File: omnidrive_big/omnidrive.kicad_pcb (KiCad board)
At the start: 2 copper layers, 165 x 87.9 mm, 73 parts, among them U1 TL072, U2 TL072

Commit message: Latest updates
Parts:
- moved R15 2.90 mm to (84.1, 49.1)
- moved R22 2.90 mm to (66.3, 48.8)
- moved R8 2.90 mm to (53.7, 57.3)
- moved C13 2.90 mm to (59.2, 55.0)
- moved R2 2.90 mm to (23.6, 56.6)
- moved R3 2.90 mm to (28.4, 49.0)
- moved R4 2.90 mm to (32.5, 49.0)
- moved R5 2.90 mm to (36.6, 56.6)
- moved U1 2.90 mm to (42.0, 49.3)
- moved U2 2.90 mm to (72.1, 49.1)
- moved J_OUT_SLV1 1.48 mm to (123.8, 56.1)
- moved J_IN_SLV1 1.45 mm to (24.0, 23.6)
- moved C7 1.30 mm to (117.5, 52.3)
- moved R16 1.30 mm to (105.5, 56.4)
- moved R19 1.30 mm to (110.4, 48.8)
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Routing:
- net Net-(J_GAIN_1-Pin_1): track 0.00 -> 90.8 mm
- net Net-(J_BLEND_2-Pin_1): track 0.00 -> 89.4 mm
- net +9V: track 0.00 -> 86.8 mm, vias 0 -> 1
- net GND: track 0.00 -> 73.6 mm, vias 0 -> 7
- net Net-(J_BLEND_3-Pin_1): track 0.00 -> 71.9 mm
- net /Vb: track 0.00 -> 57.5 mm
- net Net-(J_GAIN_2-Pin_1): track 0.00 -> 50.2 mm, vias 0 -> 1
- net Net-(J_BOOST_3-Pin_1): track 0.00 -> 43.8 mm
- net Net-(U1B-+): track 0.00 -> 39.7 mm
- net Net-(J_MODE_2-Pin_1): track 0.00 -> 38.8 mm, vias 0 -> 1
- net Net-(J_FILT_1-Pin_1): track 0.00 -> 37.3 mm
- net Net-(J_TONE_1-Pin_1): track 0.00 -> 36.4 mm
- net Net-(J_FILT_2-Pin_1): track 0.00 -> 36.3 mm
- net Net-(D1-A): track 0.00 -> 35.7 mm
- net Net-(U1B--): track 0.00 -> 34.6 mm
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- added copper zone on F.Cu, net GND

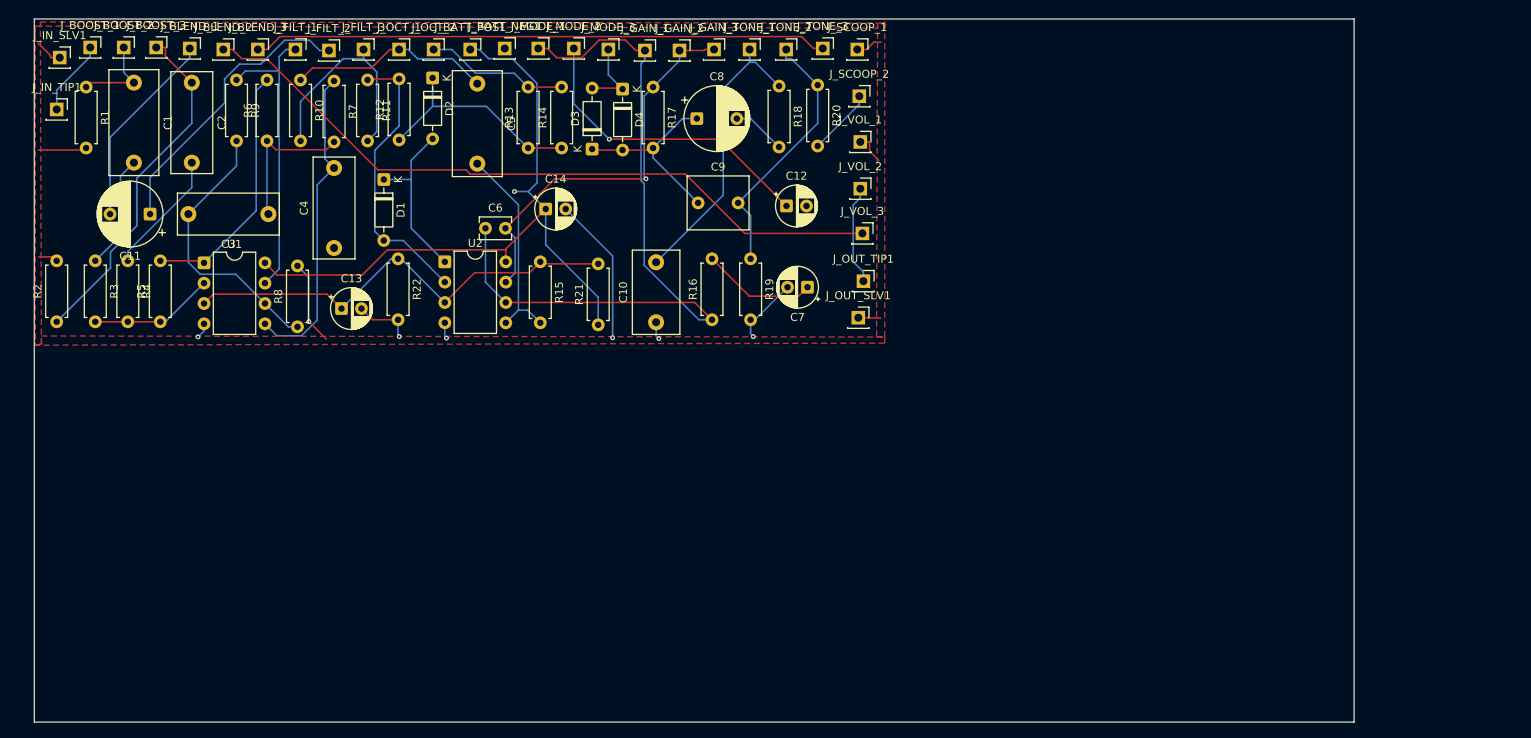
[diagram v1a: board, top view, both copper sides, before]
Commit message: my own layout, components placed
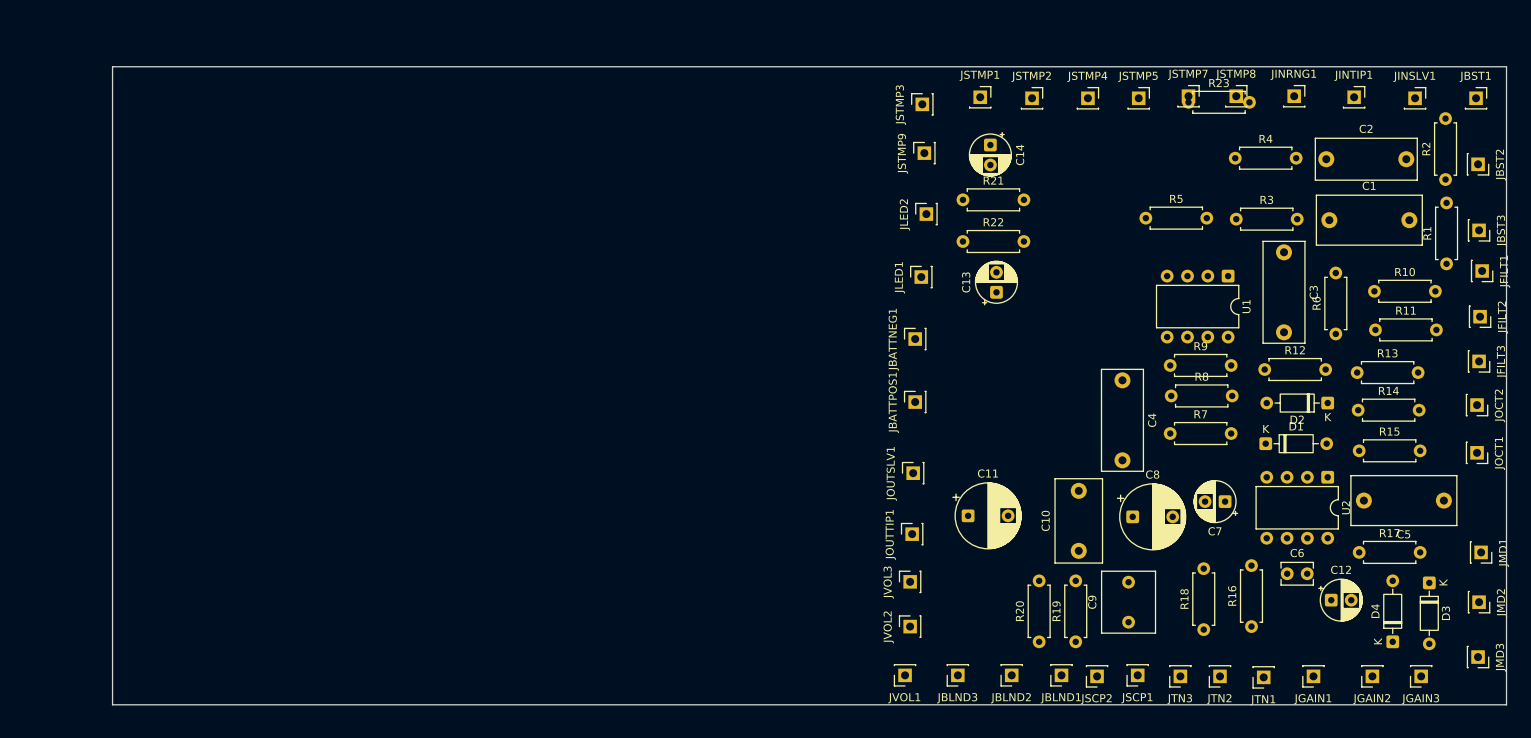
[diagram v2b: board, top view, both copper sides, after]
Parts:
- removed J_BATT_NEG1, J_BATT_POS1, J_BLEND_1, J_BLEND_2, J_BLEND_3, J_BOOST_1, J_BOOST_2, J_BOOST_3, J_FILT_1, J_FILT_2, J_FILT_3, J_GAIN_1, J_GAIN_2, J_GAIN_3, J_IN_SLV1, J_IN_TIP1, J_MODE_1, J_MODE_2, J_MODE_3, J_OCT_1, J_OCT_2, J_OUT_SLV1, J_OUT_TIP1, J_SCOOP_1, J_SCOOP_2, J_TONE_1, J_TONE_2, J_TONE_3, J_VOL_1, J_VOL_2, J_VOL_3: Conn_01x01_Pin, Connector_PinSocket_2.54mm:PinSocket_1x01_P2.54mm_Vertical
- added JBATTNEG1: Conn_01x01_Pin, Connector_PinSocket_2.54mm:PinSocket_1x01_P2.54mm_Vertical, F.Cu at (130.9, 58.8)
- added JBATTPOS1: Conn_01x01_Pin, Connector_PinSocket_2.54mm:PinSocket_1x01_P2.54mm_Vertical, F.Cu at (130.9, 66.7)
- added JBLND1: Conn_01x01_Pin, Connector_PinSocket_2.54mm:PinSocket_1x01_P2.54mm_Vertical, F.Cu at (149.2, 100.8)
- added JBLND2: Conn_01x01_Pin, Connector_PinSocket_2.54mm:PinSocket_1x01_P2.54mm_Vertical, F.Cu at (143.0, 100.8)
- added JBLND3: Conn_01x01_Pin, Connector_PinSocket_2.54mm:PinSocket_1x01_P2.54mm_Vertical, F.Cu at (136.3, 100.8)
- added JBST1: Conn_01x01_Pin, Connector_PinSocket_2.54mm:PinSocket_1x01_P2.54mm_Vertical, F.Cu at (201.0, 28.7)
- added JBST2: Conn_01x01_Pin, Connector_PinSocket_2.54mm:PinSocket_1x01_P2.54mm_Vertical, F.Cu at (201.3, 37.0)
- added JBST3: Conn_01x01_Pin, Connector_PinSocket_2.54mm:PinSocket_1x01_P2.54mm_Vertical, F.Cu at (201.4, 45.2)
- added JFILT1: Conn_01x01_Pin, Connector_PinSocket_2.54mm:PinSocket_1x01_P2.54mm_Vertical, F.Cu at (201.8, 50.3)
- added JFILT2: Conn_01x01_Pin, Connector_PinSocket_2.54mm:PinSocket_1x01_P2.54mm_Vertical, F.Cu at (201.5, 56.0)
- added JFILT3: Conn_01x01_Pin, Connector_PinSocket_2.54mm:PinSocket_1x01_P2.54mm_Vertical, F.Cu at (201.4, 61.6)
- added JGAIN1: Conn_01x01_Pin, Connector_PinSocket_2.54mm:PinSocket_1x01_P2.54mm_Vertical, F.Cu at (180.7, 101.0)
- added JGAIN2: Conn_01x01_Pin, Connector_PinSocket_2.54mm:PinSocket_1x01_P2.54mm_Vertical, F.Cu at (188.1, 101.0)
- added JGAIN3: Conn_01x01_Pin, Connector_PinSocket_2.54mm:PinSocket_1x01_P2.54mm_Vertical, F.Cu at (194.2, 101.0)
- added JINRNG1: Conn_01x01_Pin, Connector_PinSocket_2.54mm:PinSocket_1x01_P2.54mm_Vertical, F.Cu at (178.3, 28.4)
- added JINSLV1: Conn_01x01_Pin, Connector_PinSocket_2.54mm:PinSocket_1x01_P2.54mm_Vertical, F.Cu at (193.4, 28.7)
- added JINTIP1: Conn_01x01_Pin, Connector_PinSocket_2.54mm:PinSocket_1x01_P2.54mm_Vertical, F.Cu at (185.8, 28.6)
- added JLED1: Conn_01x01_Pin, Connector_PinSocket_2.54mm:PinSocket_1x01_P2.54mm_Vertical, F.Cu at (131.7, 51.1)
- added JLED2: Conn_01x01_Pin, Connector_PinSocket_2.54mm:PinSocket_1x01_P2.54mm_Vertical, F.Cu at (132.3, 43.2)
- added JMD1: Conn_01x01_Pin, Connector_PinSocket_2.54mm:PinSocket_1x01_P2.54mm_Vertical, F.Cu at (201.7, 85.5)
- added JMD2: Conn_01x01_Pin, Connector_PinSocket_2.54mm:PinSocket_1x01_P2.54mm_Vertical, F.Cu at (201.4, 91.7)
- added JMD3: Conn_01x01_Pin, Connector_PinSocket_2.54mm:PinSocket_1x01_P2.54mm_Vertical, F.Cu at (201.3, 98.6)
- added JOCT1: Conn_01x01_Pin, Connector_PinSocket_2.54mm:PinSocket_1x01_P2.54mm_Vertical, F.Cu at (201.2, 73.0)
- added JOCT2: Conn_01x01_Pin, Connector_PinSocket_2.54mm:PinSocket_1x01_P2.54mm_Vertical, F.Cu at (201.2, 67.1)
- added JOUTSLV1: Conn_01x01_Pin, Connector_PinSocket_2.54mm:PinSocket_1x01_P2.54mm_Vertical, F.Cu at (130.7, 75.6)
- added JOUTTIP1: Conn_01x01_Pin, Connector_PinSocket_2.54mm:PinSocket_1x01_P2.54mm_Vertical, F.Cu at (130.6, 83.2)
- added JSCP1: Conn_01x01_Pin, Connector_PinSocket_2.54mm:PinSocket_1x01_P2.54mm_Vertical, F.Cu at (158.8, 100.8)
- added JSCP2: Conn_01x01_Pin, Connector_PinSocket_2.54mm:PinSocket_1x01_P2.54mm_Vertical, F.Cu at (153.7, 101.0)
- added JSTMP1: Conn_01x01_Pin, Connector_PinSocket_2.54mm:PinSocket_1x01_P2.54mm_Vertical, F.Cu at (139.1, 28.6)
- added JSTMP2: Conn_01x01_Pin, Connector_PinSocket_2.54mm:PinSocket_1x01_P2.54mm_Vertical, F.Cu at (145.5, 28.7)
- added JSTMP3: Conn_01x01_Pin, Connector_PinSocket_2.54mm:PinSocket_1x01_P2.54mm_Vertical, F.Cu at (131.8, 29.5)
- added JSTMP4: Conn_01x01_Pin, Connector_PinSocket_2.54mm:PinSocket_1x01_P2.54mm_Vertical, F.Cu at (152.5, 28.7)
- added JSTMP5: Conn_01x01_Pin, Connector_PinSocket_2.54mm:PinSocket_1x01_P2.54mm_Vertical, F.Cu at (158.9, 28.7)
- added JSTMP7: Conn_01x01_Pin, Connector_PinSocket_2.54mm:PinSocket_1x01_P2.54mm_Vertical, F.Cu at (165.1, 28.4)
- added JSTMP8: Conn_01x01_Pin, Connector_PinSocket_2.54mm:PinSocket_1x01_P2.54mm_Vertical, F.Cu at (171.1, 28.4)
- added JSTMP9: Conn_01x01_Pin, Connector_PinSocket_2.54mm:PinSocket_1x01_P2.54mm_Vertical, F.Cu at (132.1, 35.6)
- added JTN1: Conn_01x01_Pin, Connector_PinSocket_2.54mm:PinSocket_1x01_P2.54mm_Vertical, F.Cu at (174.5, 101.1)
- added JTN2: Conn_01x01_Pin, Connector_PinSocket_2.54mm:PinSocket_1x01_P2.54mm_Vertical, F.Cu at (169.0, 101.0)
- added JTN3: Conn_01x01_Pin, Connector_PinSocket_2.54mm:PinSocket_1x01_P2.54mm_Vertical, F.Cu at (164.1, 101.0)
- added JVOL1: Conn_01x01_Pin, Connector_PinSocket_2.54mm:PinSocket_1x01_P2.54mm_Vertical, F.Cu at (129.7, 100.8)
- added JVOL2: Conn_01x01_Pin, Connector_PinSocket_2.54mm:PinSocket_1x01_P2.54mm_Vertical, F.Cu at (130.3, 94.7)
- added JVOL3: Conn_01x01_Pin, Connector_PinSocket_2.54mm:PinSocket_1x01_P2.54mm_Vertical, F.Cu at (130.3, 89.2)
- added R23: 10K, Resistor_THT:R_Axial_DIN0207_L6.3mm_D2.5mm_P7.62mm_Horizontal, F.Cu at (165.1, 29.2)
- moved R2 174.5 mm to (197.2, 38.9)
- moved R1 171.5 mm to (197.4, 49.4), turned to 90 degrees
- moved C1 150.4 mm to (182.7, 43.9), turned to 0 degrees
- moved R3 142.7 mm to (171.1, 43.8), turned to 0 degrees
- moved C2 142.1 mm to (182.3, 36.3), turned to 0 degrees
- moved R4 139.0 mm to (170.9, 36.2), turned to 0 degrees
- moved R10 136.8 mm to (188.3, 52.8), turned to 0 degrees
- moved R6 135.8 mm to (183.5, 58.2)
- moved C5 131.6 mm to (197.0, 79.0), turned to 180 degrees
- moved R11 129.8 mm to (188.5, 57.7), turned to 0 degrees
- moved U1 128.0 mm to (170.1, 50.9), turned to -90 degrees
- moved C3 127.0 mm to (177.0, 48.0), turned to -90 degrees
- moved R5 123.9 mm to (159.8, 43.7), turned to 0 degrees
- moved R9 122.0 mm to (162.8, 62.1), turned to 0 degrees
- moved D2 119.0 mm to (182.5, 66.8), turned to 180 degrees
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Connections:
- C11 pad 1: Net-(J_FILT_2-Pin_1) -> Net-(JFILT2-Pin_1)
- R5 pad 2: Net-(R5-Pad2) -> Net-(JFILT2-Pin_1)
- R6 pad 2: Net-(R5-Pad2) -> Net-(JFILT2-Pin_1)
- U1 pad 1: Net-(R5-Pad2) -> Net-(JFILT2-Pin_1)
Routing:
- net Net-(JGAIN1-Pin_1): track 90.8 -> 0.00 mm
- net Net-(J_BLEND_2-Pin_1): track 89.4 -> 0.00 mm
- net +9V: track 86.8 -> 0.00 mm, vias 1 -> 0
- net GND: track 73.6 -> 0.00 mm, vias 7 -> 0
- net Net-(J_BLEND_3-Pin_1): track 71.9 -> 0.00 mm
- net /Vb: track 57.5 -> 0.00 mm
- net Net-(JGAIN2-Pin_1): track 50.2 -> 0.00 mm, vias 1 -> 0
- net Net-(JBST3-Pin_1): track 43.8 -> 0.00 mm
- net Net-(U1B-+): track 39.7 -> 0.00 mm
- net Net-(JMD1-Pin_1): track 38.8 -> 0.00 mm, vias 1 -> 0
- net Net-(JFILT1-Pin_1): track 37.3 -> 0.00 mm
- net Net-(JTN1-Pin_1): track 36.4 -> 0.00 mm
- net Net-(J_FILT_2-Pin_1): track 36.3 -> 0.00 mm
- net Net-(D1-A): track 35.7 -> 0.00 mm
- net Net-(U1B--): track 34.6 -> 0.00 mm
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- removed copper zone on F.Cu, net GND
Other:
- board size 165 x 87.9 mm -> 174.2 x 79.8 mm

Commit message: placed + routed everything except ground plane
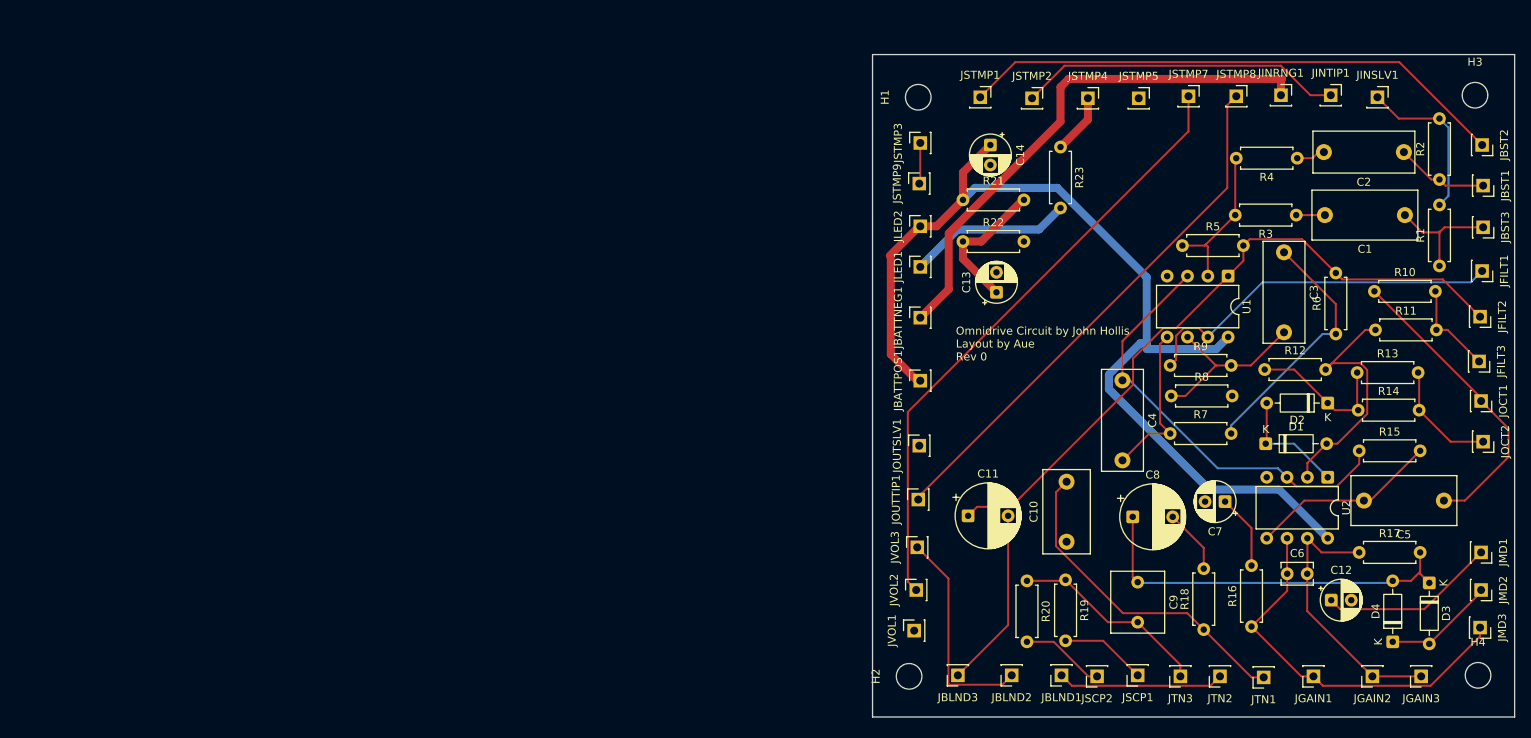
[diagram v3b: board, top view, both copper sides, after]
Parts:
- added H1: MountingHole, MountingHole:MountingHole_3.2mm_M3, F.Cu at (131.3, 28.6)
- added H2: MountingHole, MountingHole:MountingHole_3.2mm_M3, F.Cu at (130.2, 101.0)
- added H3: MountingHole, MountingHole:MountingHole_3.2mm_M3, F.Cu at (200.9, 28.3)
- added H4: MountingHole, MountingHole:MountingHole_3.2mm_M3, F.Cu at (201.3, 100.8)
- moved R23 16.9 mm to (149.1, 34.8), turned to -90 degrees
- moved C2 9.74 mm to (192.0, 35.4), turned to 180 degrees
- moved C1 9.47 mm to (192.2, 43.3), turned to 180 degrees
- moved JBST3 7.90 mm to (201.9, 44.8)
- moved R19 7.85 mm to (149.7, 88.9), turned to -90 degrees
- moved R20 7.77 mm to (144.9, 89.0), turned to -90 degrees
- moved R4 7.75 mm to (178.7, 36.2), turned to 180 degrees
- moved R3 7.51 mm to (178.6, 43.3), turned to 180 degrees
- moved JOCT1 6.50 mm to (201.7, 66.5)
- moved JBST2 5.89 mm to (201.8, 34.5), turned to -90 degrees
- moved R5 5.71 mm to (164.3, 47.1)
- moved JVOL1 5.70 mm to (130.8, 95.2), turned to 90 degrees
- moved JBST1 5.61 mm to (201.9, 39.6)
- moved C9 5.13 mm to (158.8, 89.2), turned to -90 degrees
- moved JSTMP3 4.83 mm to (131.6, 34.3)
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- renumbered JBST3 to JBST1, JBST1 to JBST2, JBST2 to JBST3
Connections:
- C12 pad 2: unconnected-(C12-Pad2) -> GND
- C4 pad 1: unconnected-(C4-Pad1) -> /Vb
- JBST2 pad 1: Net-(JBST1-Pin_1) (its old number) -> Net-(JBST2-Pin_1)
- JINTIP1 pad 1: Net-(JBST1-Pin_1) (its old number) -> Net-(JINTIP1-Pin_1)
- JSTMP1 pad 1: Net-(JBST1-Pin_1) (its old number) -> Net-(JBST2-Pin_1)
- JSTMP2 pad 1: Net-(JSTMP2-Pin_1) -> Net-(JINTIP1-Pin_1)
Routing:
- net +9V: track 0.00 -> 129.0 mm
- net Net-(JFILT2-Pin_1): track 0.00 -> 85.4 mm
- net /EFFECT_OUT: track 0.00 -> 76.7 mm
- net /Vb: track 0.00 -> 72.1 mm
- net Net-(JBST2-Pin_1): track 0.00 -> 68.8 mm
- net Net-(JOUTTIP1-Pin_1): track 0.00 -> 66.9 mm
- net Net-(JBATTNEG1-Pin_1): track 0.00 -> 66.3 mm
- net Net-(D3-K): track 0.00 -> 48.6 mm
- net Net-(JGAIN1-Pin_1): track 0.00 -> 48.2 mm
- net Net-(JFILT1-Pin_1): track 0.00 -> 46.6 mm
- net Net-(JTN1-Pin_1): track 0.00 -> 41.4 mm
- net Net-(JINTIP1-Pin_1): track 0.00 -> 40.5 mm
- net Net-(JOCT1-Pin_1): track 0.00 -> 38.0 mm
- net Net-(JGAIN2-Pin_1): track 0.00 -> 34.0 mm
- net Net-(C3-Pad1): track 0.00 -> 31.7 mm
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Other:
- board size 174.2 x 79.8 mm -> 80.3 x 82.8 mm
- board text added: "Omnidrive Circuit by John Hollis Layout by Aue Rev 0"

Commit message: fix checks
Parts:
- moved JSTMP8 41.2 mm to (131.6, 40.3), turned to 90 degrees
- moved JSTMP7 34.1 mm to (131.6, 34.5), turned to 90 degrees
- moved JSTMP1 26.4 mm to (165.5, 28.6)
- moved JSTMP2 26.0 mm to (171.6, 28.3)
- moved JSTMP3 15.2 mm to (145.7, 28.7), turned to 0 degrees
- moved JSTMP9 13.6 mm to (140.0, 28.7), turned to 0 degrees
- moved JVOL2 13.6 mm to (131.4, 76.6)
- moved JOUTSLV1 10.4 mm to (131.2, 82.5)
- moved JOUTTIP1 7.11 mm to (131.4, 71.8)
- moved JVOL3 4.35 mm to (130.7, 89.2)
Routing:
- net Net-(JOUTTIP1-Pin_1): track 66.9 -> 35.5 mm
- net /EFFECT_OUT: track 76.7 -> 47.9 mm
- net Net-(JBST2-Pin_1): track 68.8 -> 42.2 mm
- net Net-(JINTIP1-Pin_1): track 40.5 -> 16.1 mm
- net GND: track 31.4 -> 8.85 mm
- net /Vb: track 72.1 -> 90.5 mm
- net Net-(JBLND2-Pin_1): track 27.2 -> 23.1 mm
- net Net-(JSTMP3-Pin_1): track 5.13 -> 5.72 mm
- added copper zone on B.Cu, net GND

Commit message: fixed unconnected pin
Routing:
- net GND: track 8.85 -> 17.8 mm
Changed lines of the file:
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@@
+	)
+	(segment
+		(start 170.215 76.078)
+		(end 167.172 79.121)
+		(width 1)
+		(layer "F.Cu")
+		(net "GND")
 	)
 	(segment
@@
 		(layer "F.Cu")
 		(net "GND")
+	)
+	(segment
+		(start 174.879 76.078)
+		(end 170.215 76.078)
+		(width 1)
+		(layer "F.Cu")
+		(net "GND")
